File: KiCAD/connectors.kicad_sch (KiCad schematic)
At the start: 14 parts, among them J2 USB4105-GF-A, J3 Conn_02x05_Odd_Even, J5 Conn_01x02, J6 Conn_01x04, J7 STX-3120-5B-284C

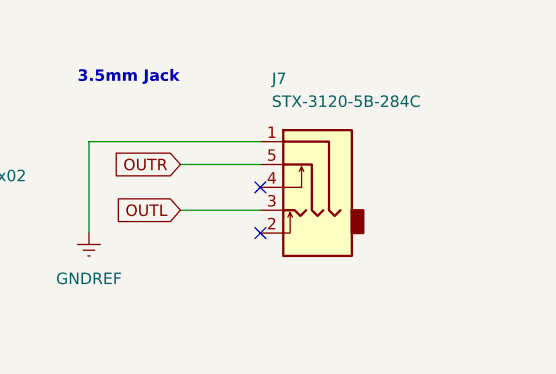
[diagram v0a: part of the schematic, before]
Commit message: Fixing 3.3V being fed to VDDCORE. Swaping 3.3V LDOs to onsemi ones with higher output current
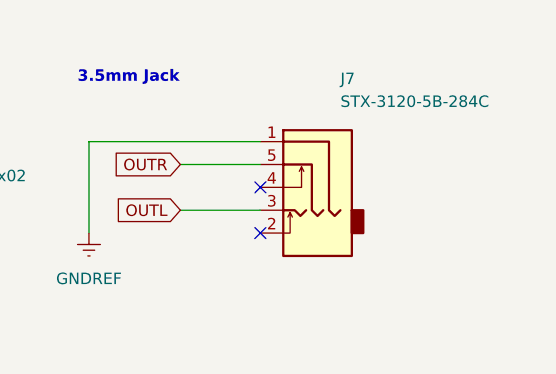
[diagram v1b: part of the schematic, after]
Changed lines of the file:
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@@
   (symbol (lib_id "Connector:AudioJack3_SwitchTR") (at 229.87 30.48 0) (mirror y) (unit 1)
     (in_bom yes) (on_board yes) (fields_autoplaced)
-    (property "Reference" "J7" (id 0) (at 226.06 20.9549 0)
+    (property "Reference" "J7" (id 0) (at 233.68 20.9549 0)
       (effects (font (size 1.27 1.27)) (justify right))
     )
-    (property "Value" "STX-3120-5B-284C" (id 1) (at 226.06 23.4949 0)
+    (property "Value" "STX-3120-5B-284C" (id 1) (at 233.68 23.4949 0)
       (effects (font (size 1.27 1.27)) (justify right))
     )
-    (property "Footprint" "SamacSys_Parts:STX31205B284C" (id 2) (at 233.68 19.05 0)
+    (property "Footprint" "SamacSys_Parts:STX31205B284C" (id 2) (at 226.06 19.05 0)
       (effects (font (size 1.27 1.27)) hide)
     )
-    (property "Datasheet" "~" (id 3) (at 233.68 19.05 0)
+    (property "Datasheet" "~" (id 3) (at 226.06 19.05 0)
       (effects (font (size 1.27 1.27)) hide)
     )

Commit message: Adding stuff for rev 2.0
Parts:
- added FB4: 0R, SamacSys_Parts:BEADC2012X110N, symbol Device:FerriteBead
- added H2, H3, H4, H5: MountingHole_Pad, MountingHole:MountingHole_2.2mm_M2_DIN965_Pad_TopBottom, symbol Mechanical:MountingHole_Pad
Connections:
- net +5V: now also FB4.1; no longer JP3.2 (C)
- new net: FB4.2, JP3.2 (C)
- no-connect marks 5 -> 9
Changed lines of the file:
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@@
   (no_connect (at 41.91 144.78))
   (no_connect (at 41.91 40.64))
+  (no_connect (at 218.44 146.05))
+  (no_connect (at 195.58 146.05))
+  (no_connect (at 264.16 146.05))
+  (no_connect (at 241.3 146.05))
   (no_connect (at 224.79 33.02))
   (no_connect (at 224.79 38.1))
@@
     (stroke (width 0) (type default) (color 0 0 0 0))
   )
-  (wire (pts (xy 149.86 40.64) (xy 162.56 40.64))
+  (wire (pts (xy 149.86 40.64) (xy 152.4 40.64))
     (stroke (width 0) (type default) (color 0 0 0 0))
   )
@@
   )
   (wire (pts (xy 48.26 60.96) (xy 48.26 38.1))
+    (stroke (width 0) (type default) (color 0 0 0 0))
+  )
+  (wire (pts (xy 160.02 40.64) (xy 162.56 40.64))
     (stroke (width 0) (type default) (color 0 0 0 0))
   )
@@
     (pin "1")
   )
+  (symbol (lib_id "Mechanical:MountingHole_Pad") (at 218.44 143.51 0) (unit 1)
+    (in_bom yes) (on_board yes) (fields_autoplaced)
+    (property "Reference" "H3" (id 0) (at 220.98 140.9699 0)
+      (effects (font (size 1.27 1.27)) (justify left))
+    )
+    (property "Value" "MountingHole_Pad" (id 1) (at 220.98 143.5099 0)
+      (effects (font (size 1.27 1.27)) (justify left))
+    )
+    (property "Footprint" "MountingHole:MountingHole_2.2mm_M2_DIN965_Pad_TopBottom" (id 2) (at 218.44 143.51 0)
+      (effects (font (size 1.27 1.27)) hide)
+    )
+    (property "Datasheet" "~" (id 3) (at 218.44 143.51 0)
+      (effects (font (size 1.27 1.27)) hide)
+    )
+    (pin "1")
+  )
   (symbol (lib_id "Type-C:HRO-TYPE-C-31-M-12") (at 39.37 49.53 0) (unit 1)
     (in_bom yes) (on_board yes) (fields_autoplaced)
@@
     (pin "1")
   )
+  (symbol (lib_id "Mechanical:MountingHole_Pad") (at 241.3 143.51 0) (unit 1)
+    (in_bom yes) (on_board yes) (fields_autoplaced)
+    (property "Reference" "H4" (id 0) (at 243.84 140.9699 0)
+      (effects (font (size 1.27 1.27)) (justify left))
+    )
+    (property "Value" "MountingHole_Pad" (id 1) (at 243.84 143.5099 0)
+      (effects (font (size 1.27 1.27)) (justify left))
+    )
+    (property "Footprint" "MountingHole:MountingHole_2.2mm_M2_DIN965_Pad_TopBottom" (id 2) (at 241.3 143.51 0)
+      (effects (font (size 1.27 1.27)) hide)
+    )
+    (property "Datasheet" "~" (id 3) (at 241.3 143.51 0)
+      (effects (font (size 1.27 1.27)) hide)
+    )
+    (pin "1")
+  )
   (symbol (lib_id "Connector_Generic:Conn_01x04") (at 201.93 97.79 0) (unit 1)
     (in_bom yes) (on_board yes) (fields_autoplaced)
@@
     (pin "3")
     (pin "4")
+  )
+  (symbol (lib_id "Mechanical:MountingHole_Pad") (at 195.58 143.51 0) (unit 1)
+    (in_bom yes) (on_board yes) (fields_autoplaced)
+    (property "Reference" "H2" (id 0) (at 198.12 140.9699 0)
+      (effects (font (size 1.27 1.27)) (justify left))
+    )
+    (property "Value" "MountingHole_Pad" (id 1) (at 198.12 143.5099 0)
+      (effects (font (size 1.27 1.27)) (justify left))
+    )
+    (property "Footprint" "MountingHole:MountingHole_2.2mm_M2_DIN965_Pad_TopBottom" (id 2) (at 195.58 143.51 0)
+      (effects (font (size 1.27 1.27)) hide)
+    )
+    (property "Datasheet" "~" (id 3) (at 195.58 143.51 0)
+      (effects (font (size 1.27 1.27)) hide)
+    )
+    (pin "1")
   )
   (symbol (lib_id "power:GND") (at 60.96 63.5 0) (unit 1)
@@
     (pin "1")
   )
+  (symbol (lib_id "Mechanical:MountingHole_Pad") (at 264.16 143.51 0) (unit 1)
+    (in_bom yes) (on_board yes) (fields_autoplaced)
+    (property "Reference" "H5" (id 0) (at 266.7 140.9699 0)
+      (effects (font (size 1.27 1.27)) (justify left))
+    )
+    (property "Value" "MountingHole_Pad" (id 1) (at 266.7 143.5099 0)
+      (effects (font (size 1.27 1.27)) (justify left))
+    )
+    (property "Footprint" "MountingHole:MountingHole_2.2mm_M2_DIN965_Pad_TopBottom" (id 2) (at 264.16 143.51 0)
+      (effects (font (size 1.27 1.27)) hide)
+    )
+    (property "Datasheet" "~" (id 3) (at 264.16 143.51 0)
+      (effects (font (size 1.27 1.27)) hide)
+    )
+    (pin "1")
+  )
   (symbol (lib_id "power:+3.3V") (at 34.29 133.35 0) (unit 1)
     (in_bom yes) (on_board yes) (fields_autoplaced)
@@
     (pin "1")
   )
+  (symbol (lib_id "Device:FerriteBead") (at 156.21 40.64 90) (unit 1)
+    (in_bom yes) (on_board yes) (fields_autoplaced)
+    (property "Reference" "FB4" (id 0) (at 156.1592 33.02 90))
+    (property "Value" "0R" (id 1) (at 156.1592 35.56 90))
+    (property "Footprint" "SamacSys_Parts:BEADC2012X110N" (id 2) (at 156.21 42.418 90)
+      (effects (font (size 1.27 1.27)) hide)
+    )
+    (property "Datasheet" "~" (id 3) (at 156.21 40.64 0)
+      (effects (font (size 1.27 1.27)) hide)
+    )
+    (property "Part Number" "MFBW1V2012-000-R" (id 4) (at 156.21 40.64 90)
+      (effects (font (size 1.27 1.27)) hide)
+    )
+    (property "Mouser Part Number" "704-MFBW1V2012-000-R" (id 5) (at 156.21 40.64 90)
+      (effects (font (size 1.27 1.27)) hide)
+    )
+    (pin "1")
+    (pin "2")
+  )
   (symbol (lib_id "power:VBUS") (at 116.84 35.56 0) (unit 1)
